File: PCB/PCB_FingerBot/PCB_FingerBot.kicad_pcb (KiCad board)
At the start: 2 copper layers, 3 parts, among them J1 Conn_01x02_Pin, U1 XIAO-ESP32-C6-SMD, U2 TPS61222DCK

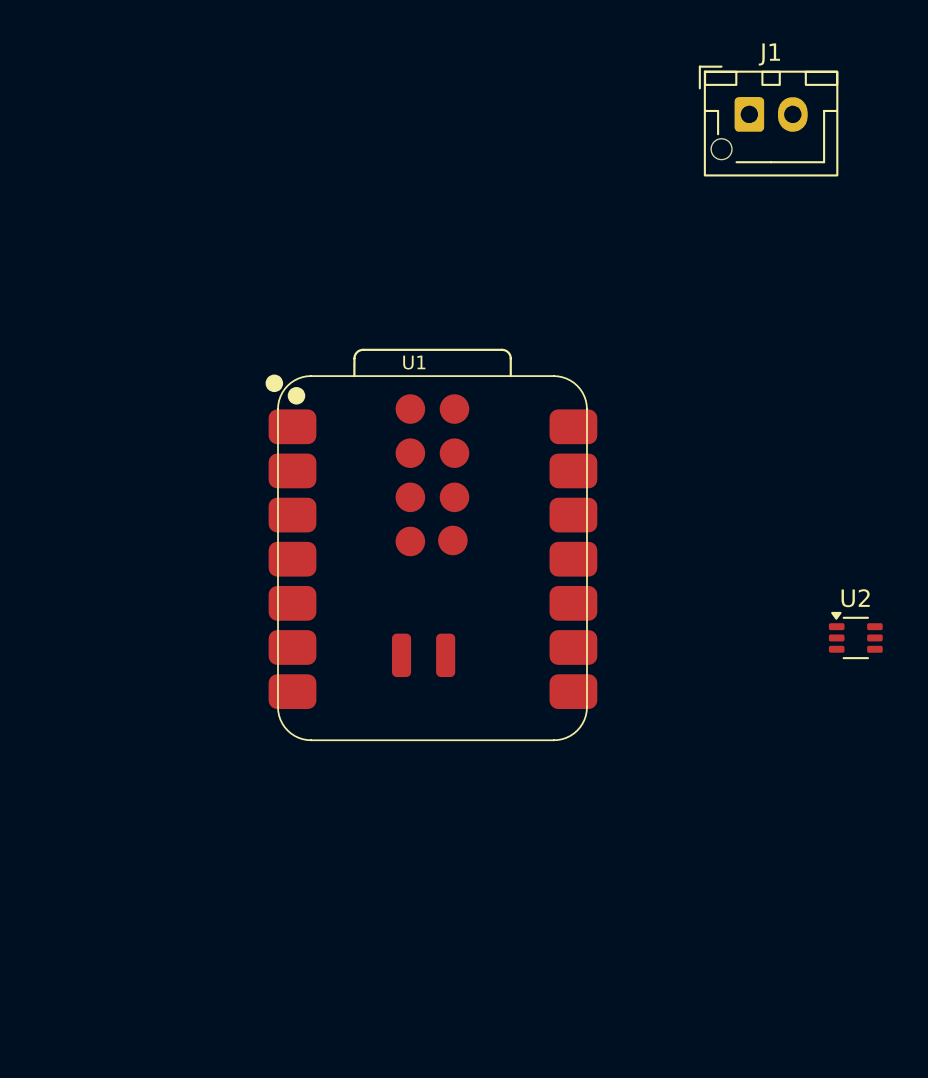
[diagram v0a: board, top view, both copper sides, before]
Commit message: Changed boost converter to a more powerful one
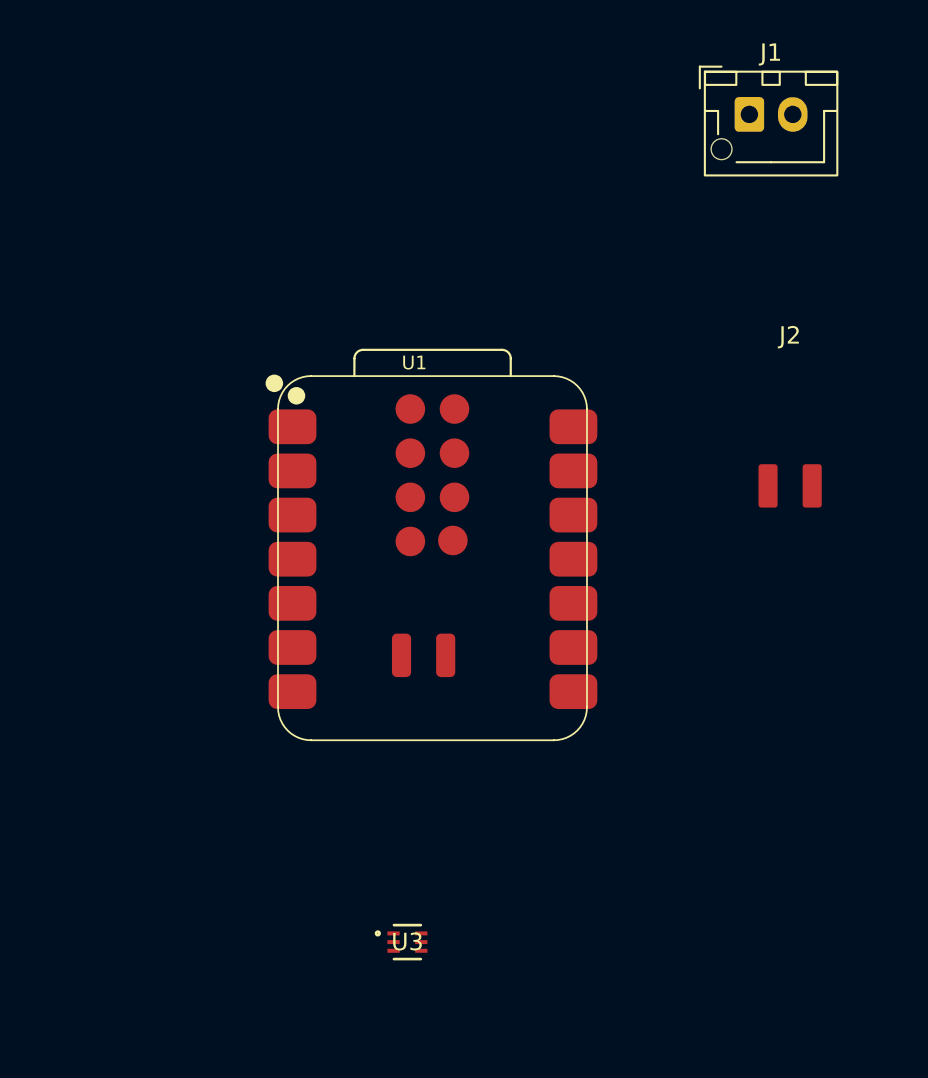
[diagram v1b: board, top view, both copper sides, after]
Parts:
- removed U2: TPS61222DCK, Package_TO_SOT_SMD:Texas_R-PDSO-G6
- added J2: Conn_2_pads, Pad connector:Pads 1x2 2.54mm Battery, F.Cu at (167.8, 91.8)
- added U3: TPS61299ADRLR, TPS61299:SOT-5X3-6_DRL_TEX, F.Cu at (145.8, 118.0)
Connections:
- U1 pad 1: unconnected-(U1-D0-Pad1) -> Servo - EN
- U1 pad 2: unconnected-(U1-D1-Pad2) -> Servo - PWM

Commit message: Update component to JLC available ones
Changed boost converter to an available reference on jlc, changed SEEED studio for through hole soldering (part not available on JLC), started other part assigne
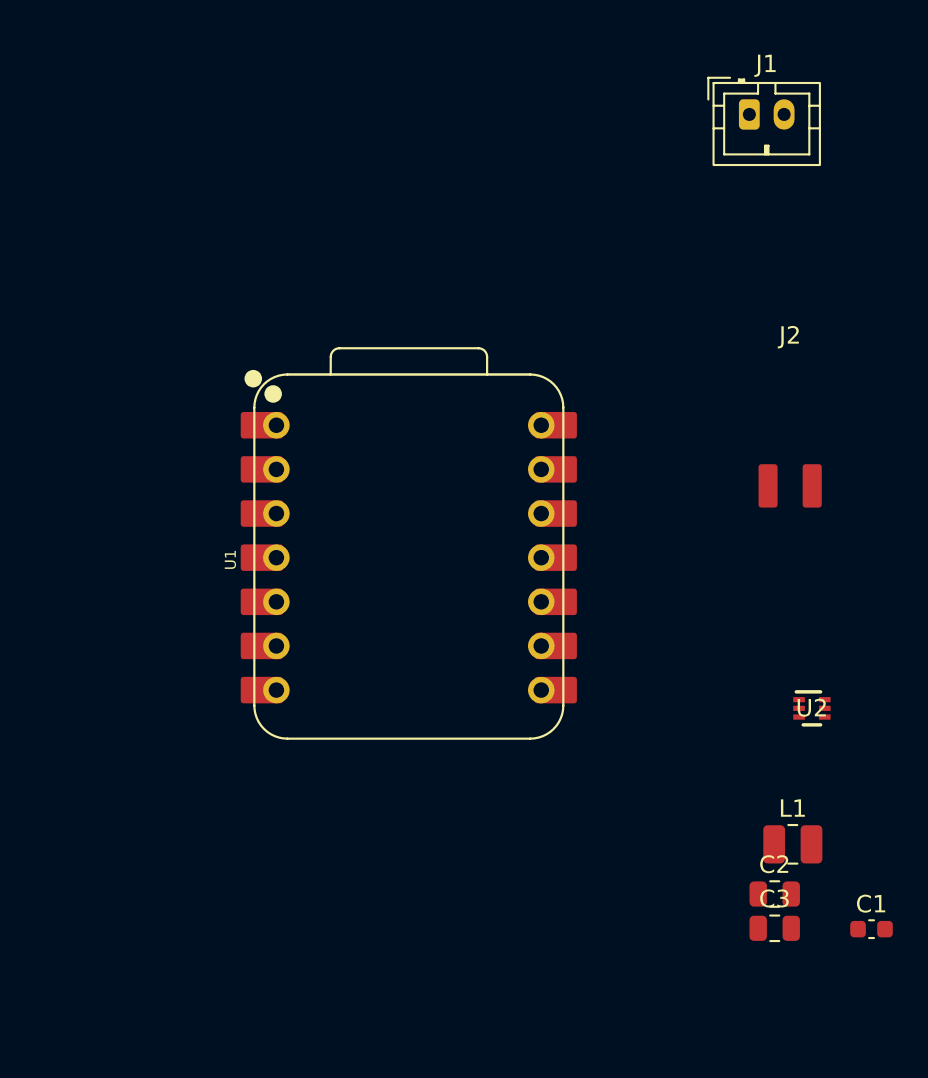
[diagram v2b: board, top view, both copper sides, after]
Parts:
- removed U3: TPS61299ADRLR, TPS61299:SOT-5X3-6_DRL_TEX
- added C1: 10 μF, Capacitor_SMD:C_0603_1608Metric, F.Cu at (172.5, 117.3)
- added C2: 22 μF, Capacitor_SMD:C_0805_2012Metric, F.Cu at (166.9, 115.2)
- added C3: 22 μF, Capacitor_SMD:C_0805_2012Metric, F.Cu at (166.9, 117.2)
- added L1: 1 μH, Inductor_SMD:L_1008_2520Metric, F.Cu at (168.0, 112.4)
- added U2: TPS61023DRLR, TPS61023DRLR:DRL0006A, F.Cu at (169.1, 104.6)
- J1: footprint Connector_JST:JST_XH_B2B-XH-AM_1x02_P2.50mm_Vertical -> Connector_JST:JST_PH_B2B-PH-K_1x02_P2.00mm_Vertical
- U1: footprint Seeed_Studio_XIAO_Series:XIAO-ESP32-C6-SMD -> Seeed_Studio_XIAO_Series:XIAO-ESP32-C6-DIP
- moved U1 13.0 mm to (145.9, 95.9), turned to 90 degrees

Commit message: Added headers for SEEED, changed components and footprints
Added mouting female pin headers on SEEED footprint, modified the passive components of the power converter, modified footprint of inductor to spec
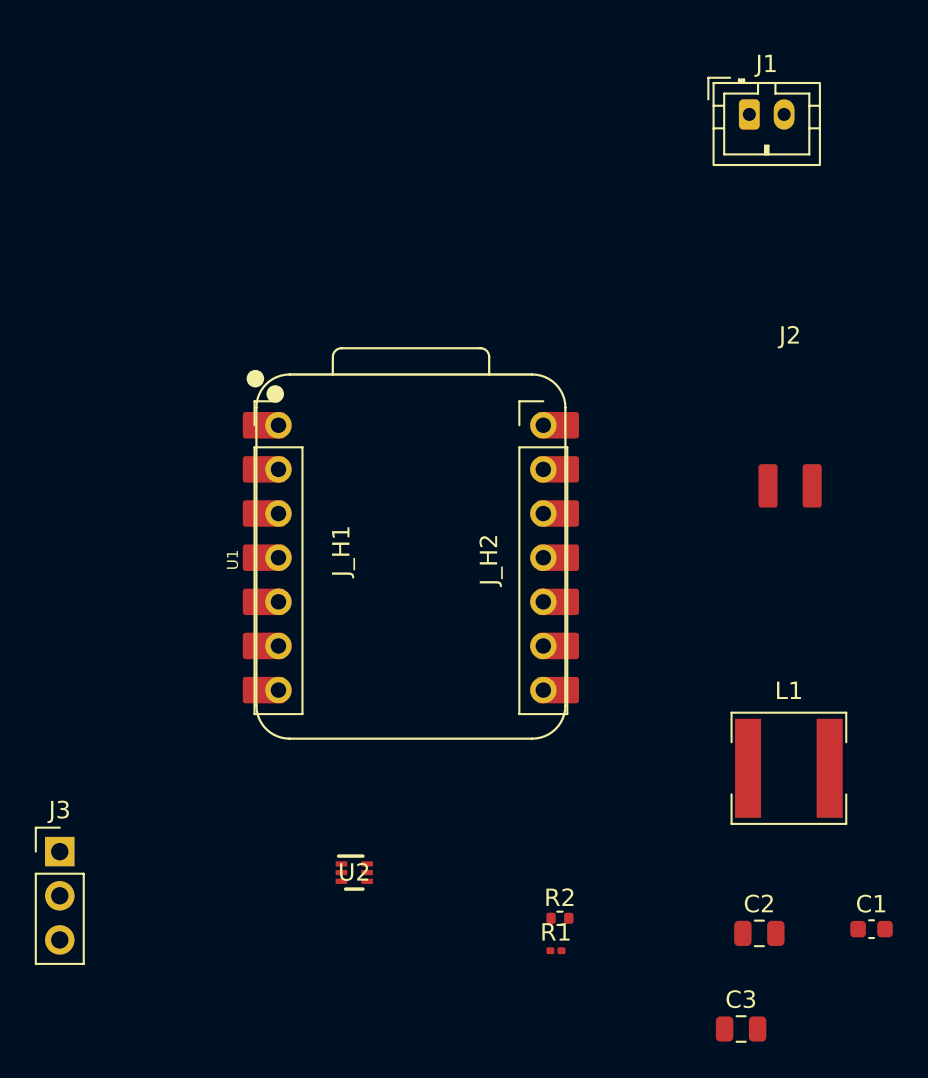
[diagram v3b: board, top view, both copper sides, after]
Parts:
- added J3: Conn_01x03_Pin, Connector_PinHeader_2.54mm:PinHeader_1x03_P2.54mm_Vertical, F.Cu at (125.8, 112.8)
- added J_H1: PinHeader_1x07_P2.54_INVISIBLE, Invisible_PinHeaders:PinHeader_1x07_P2.54_INVISIBLE, F.Cu at (138.4, 95.9)
- added J_H2: PinHeader_1x07_P2.54_INVISIBLE, Invisible_PinHeaders:PinHeader_1x07_P2.54_INVISIBLE, F.Cu at (153.6, 95.9)
- added R1: 732k, Resistor_SMD:R_0201_0603Metric, F.Cu at (154.3, 118.5)
- added R2: 100k, Resistor_SMD:R_0402_1005Metric, F.Cu at (154.6, 116.6)
- L1: value 1 μH -> 2.7 μH; footprint Inductor_SMD:L_1008_2520Metric -> Inductor_SMD:L_6.3x6.3_H3
- moved U2 28.0 mm to (142.7, 114.0)
- moved C3 6.11 mm to (165.0, 123.0)
- moved L1 4.38 mm to (167.8, 108.0)
- moved C2 2.43 mm to (166.1, 117.5)
- moved U1 0.12 mm to (146.0, 95.9)

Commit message: Made a first PCB layout + corrected battery polarity on jst connect
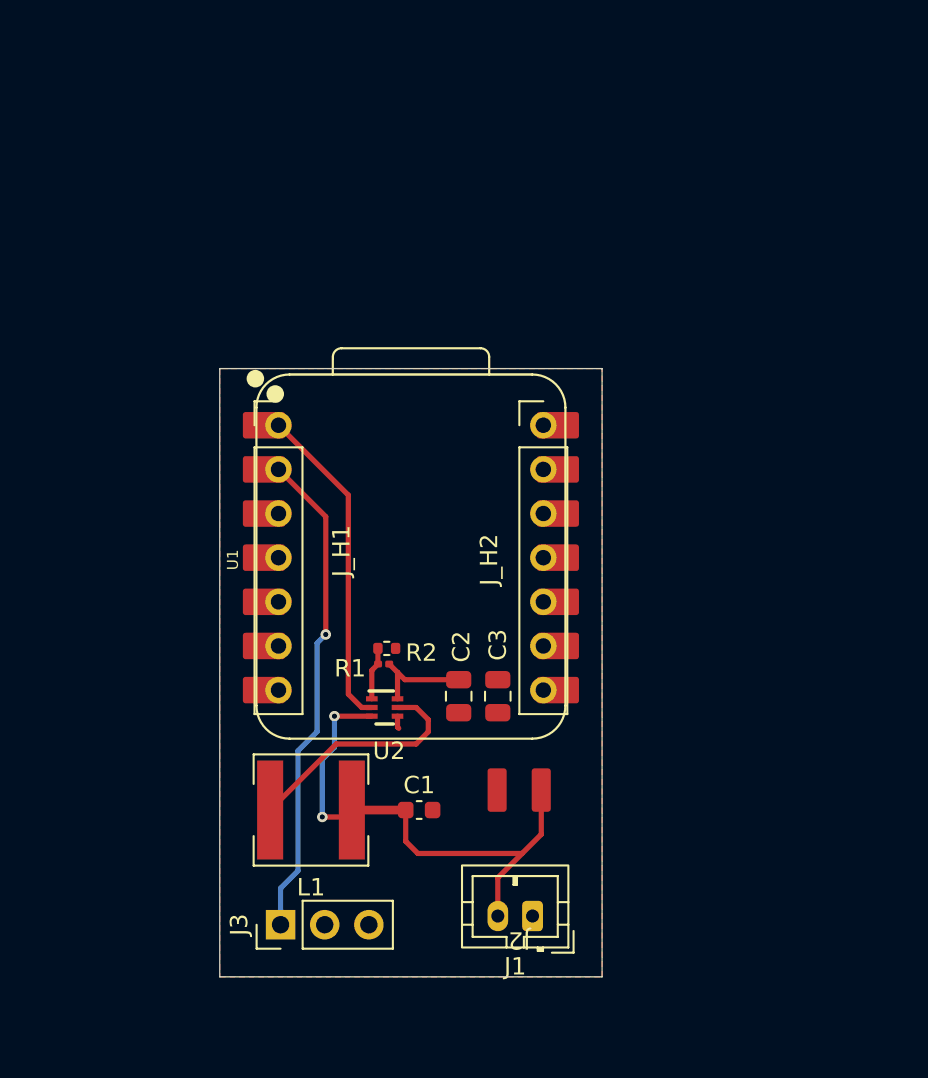
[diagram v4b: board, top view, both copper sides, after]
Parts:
- moved J1 47.8 mm to (153.0, 116.5), turned to 180 degrees
- moved L1 27.6 mm to (140.2, 110.4), turned to 180 degrees
- moved C1 26.9 mm to (146.5, 110.4)
- moved C3 23.7 mm to (151.0, 103.8), turned to -90 degrees
- moved J2 23.4 mm to (152.2, 109.2), turned to 180 degrees
- moved C2 22.0 mm to (148.8, 103.8), turned to -90 degrees
- moved R1 19.2 mm to (144.4, 102.0)
- moved R2 18.5 mm to (144.6, 101.1), turned to 180 degrees
- moved J3 13.4 mm to (138.5, 117.0), turned to 90 degrees
- moved U2 9.66 mm to (144.5, 104.5)
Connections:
- J1 pad 1: VBAT -> GND
- J1 pad 2: GND -> VBAT
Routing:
- net VBAT: track 0.00 -> 30.3 mm, vias 0 -> 2
- net Servo - PWM: track 0.00 -> 28.4 mm, vias 0 -> 1
- net Servo - EN: track 0.00 -> 18.8 mm
- net Net-(U2-SW): track 0.00 -> 13.7 mm
- net 5V - Servo: track 0.00 -> 5.89 mm
- net Net-(U2-FB): track 0.00 -> 3.05 mm
- net GND: track 0.00 -> 0.73 mm
- added copper zone on F.Cu, net GND
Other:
- board outline added: 22 x 35 mm
